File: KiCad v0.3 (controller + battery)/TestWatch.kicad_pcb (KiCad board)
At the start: 2 copper layers, 117 x 47.5 mm, 203 parts, among them J1 Conn_01x16

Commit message: Major Udpate 2
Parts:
- removed J1: Conn_01x16, Connector_PinHeader_1.00mm:PinHeader_1x16_P1.00mm_Vertical
- added Pogo2: Pogo2, WL-SMCC_0402:Untitled, F.Cu at (173.6, 99.5)
- added REF**: XTAL_MC-306_32.7680K-E0_PURE_SN, MC-306_32.7680K-E0_PURE_SN:MC-306_32.7680K-E0_PURE_SN, F.Cu at (197.0, 111.0)
- added REF**: BAT_BAT-HLD-003-SMT, BAT-HLD-003-SMT:BAT_BAT-HLD-003-SMT, F.Cu at (193.5, 92.5)
- added REF**: SW_EVQ-P7K01P_PAN, EVQ_P7K01P:EVQ_P7K01P, F.Cu at (205.5, 99.3)
- added REF**: LIR2050, WL-SMCC_0402:Untitled_1, F.Cu at (194.0, 92.5)
- moved IC** 11.9 mm to (187.5, 109.5)
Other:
- board size 117 x 47.5 mm -> 73 x 36.5 mm

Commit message: Uhm
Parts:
- removed D1, D10, D100, D101, D102, D103, D104, D105, D106, D107, D108, D109, D11, D110, D111, D112, D113, D114, D115, D116, D117, D118, D119, D12, D120, D121, D122, D123, D124, D125, D126, D127, D128, D129, D13, D130, D131, D132, D133, D134, D135, D136, D137, D138, D139, D14, D140, D141, D142, D143, D144, D145, D146, D147, D148, D149, D15, D150, D151, D152, D153, D154, D155, D156, D157, D158, D159, D16, D160, D161, D162, D163, D164, D165, D166, D167, D168, D169, D17, D170, D171, D172, D173, D174, D175, D176, D177, D178, D179, D18, D180, D181, D182, D183, D184, D185, D186, D187, D188, D189, D19, D190, D191, D192, D193, D194, D195, D196, D197, D198, D199, D2, D20, D200, D201, D21, D22, D23, D24, D25, D26, D27, D28, D29, D3, D30, D31, D32, D33, D34, D35, D36, D37, D38, D39, D4, D40, D41, D42, D43, D44, D45, D46, D47, D48, D49, D5, D50, D51, D52, D53, D54, D55, D56, D57, D58, D59, D6, D60, D61, D62, D63, D64, D65, D66, D67, D68, D69, D7, D70, D71, D72, D73, D74, D75, D76, D77, D78, D79, D8, D80, D81, D82, D83, D84, D85, D86, D87, D88, D89, D9, D90, D91, D92, D93, D94, D95, D96, D97, D98, D99: WL-SMCC_0402, WL-SMCC_0402:WL-SMCC_0402
- removed IC**: QFP80P900X900X160-32N, STM32G431KBT6:QFP80P900X900X160-32N
- removed Pogo2: Pogo2, WL-SMCC_0402:Untitled
- removed REF**: XTAL_MC-306_32.7680K-E0_PURE_SN, MC-306_32.7680K-E0_PURE_SN:MC-306_32.7680K-E0_PURE_SN
- removed REF**: BAT_BAT-HLD-003-SMT, BAT-HLD-003-SMT:BAT_BAT-HLD-003-SMT
- removed REF**: SW_EVQ-P7K01P_PAN, EVQ_P7K01P:EVQ_P7K01P
- removed REF**: LIR2050, WL-SMCC_0402:Untitled_1
- added BT1: BAT-HLD-003-SMT, BAT-HLD-003-SMT:BAT_BAT-HLD-003-SMT_CUT, F.Cu at (192.0, 93.5)
- added BUTT1: B3U-1100P, B3U_1100P:SW_B3U-1100P, F.Cu at (206.0, 99.5)
- added C1: GRM21BC81E106ME51K, GRM21BC81E106ME51K:CAPC2012X140N, F.Cu at (196.0, 115.5)
- added CHG1: MCP73832T-2ACI_OT, MCP73832T_2ACI_OT:SOT95P270X145-5N, F.Cu at (190.0, 105.4)
- added CUT1: MAX809SEUR_T, MAX809SEUR+T:MAX809SEUR+T, F.Cu at (180.1, 109.6)
- added J1: Conn_01x16, Connector_PinSocket_2.54mm:PinSocket_1x16_P2.54mm_Vertical, F.Cu at (180.5, 68.5)
- added Osc1: MC-306_32.7680K-E0_PURE_SN, MC-306_32.7680K-E0_PURE_SN:MC-306_32.7680K-E0_PURE_SN, F.Cu at (190.0, 113.0)
- added P13: ~, WL-SMCC_0402:PROGPAD, F.Cu at (206.0, 91.5)
- added P14: ~, WL-SMCC_0402:PROGPAD, F.Cu at (206.0, 94.5)
- added POGO1: ~, WL-SMCC_0402:Untitled, F.Cu at (173.1, 99.5)
- added Q1: IRLML6402, Package_TO_SOT_SMD:SOT-23, F.Cu at (184.5, 108.0)
- added R1: RN73H1JTTD5052F50, RN73H1JTTD5052F50:RN73H1JTTD5052F50, F.Cu at (185.5, 104.5)
- added R2: RN73H1JTTD5052F50, RN73H1JTTD5052F50:RN73H1JTTD5052F50, F.Cu at (206.5, 106.0)
- added R3: RN73H1JTTD5052F50, RN73H1JTTD5052F50:RN73H1JTTD5052F50, F.Cu at (182.0, 104.5)
- added REG1: TPS7A0225PDBVR, TPS7A0225PDBVR:TPS7A0225PDBVR, F.Cu at (184.4, 112.1)
- added STM1: STM32G431KBT6, STM32G431KBT6:QFP80P900X900X160-32N, F.Cu at (198.8, 108.7)
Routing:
- net A: track 79.8 -> 0.00 mm, vias 12 -> 0
- net E: track 78.5 -> 0.00 mm, vias 10 -> 0
- net B: track 77.9 -> 0.00 mm, vias 12 -> 0
- net F: track 77.5 -> 0.00 mm, vias 11 -> 0
- net G: track 76.5 -> 0.00 mm, vias 8 -> 0
- net H: track 75.0 -> 0.00 mm, vias 9 -> 0
- net C: track 74.8 -> 0.00 mm, vias 12 -> 0
- net I: track 72.8 -> 0.00 mm, vias 6 -> 0
- net J: track 72.8 -> 0.00 mm, vias 7 -> 0
- net D: track 72.5 -> 0.00 mm, vias 12 -> 0
- net L: track 71.5 -> 0.00 mm, vias 5 -> 0
- net K: track 66.4 -> 0.00 mm
- net P: track 64.9 -> 0.00 mm
- net O: track 62.5 -> 0.00 mm
- net N: track 60.1 -> 0.00 mm
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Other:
- board size 73 x 36.5 mm -> 45 x 52 mm

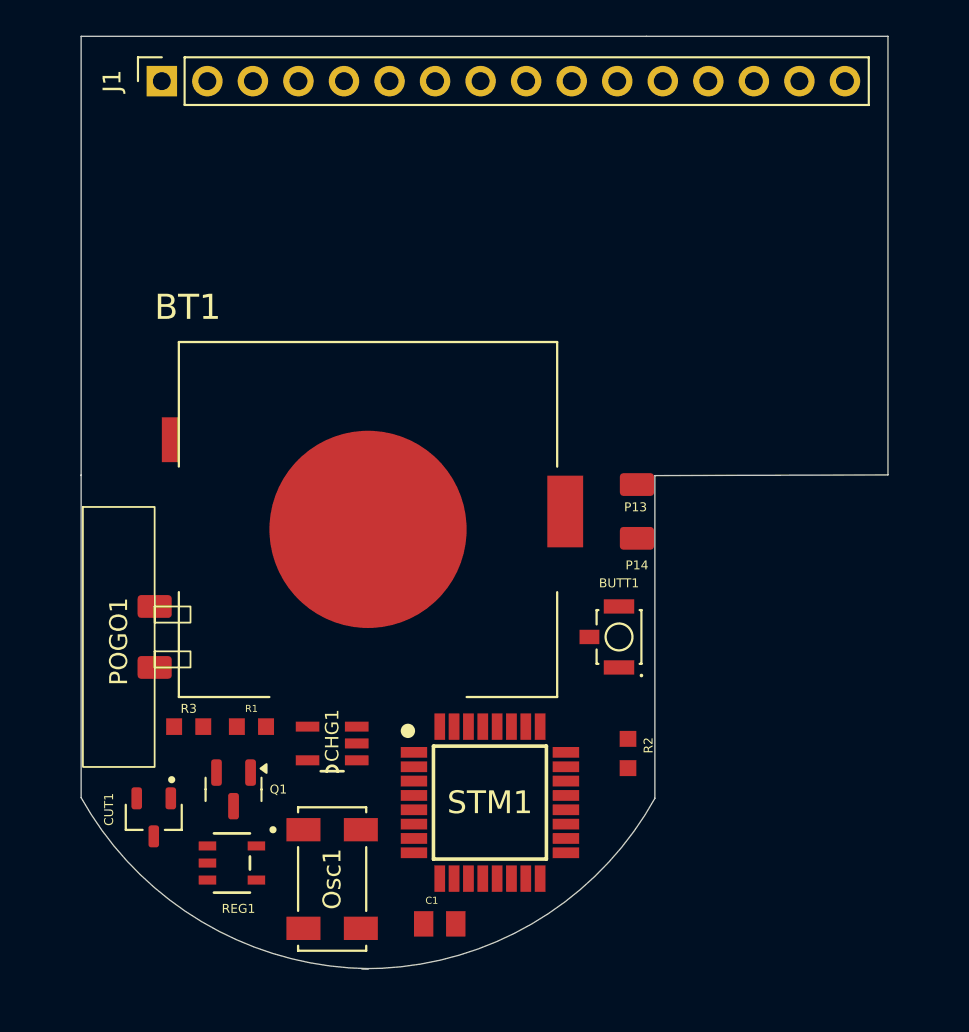
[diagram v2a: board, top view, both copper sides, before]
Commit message: v0.3 sent for fab, v0.4 still in progress
v0.3 and v0.4 have the same component footprints - that way, I only need to have 1 stencil (if v0.3 works!!!)
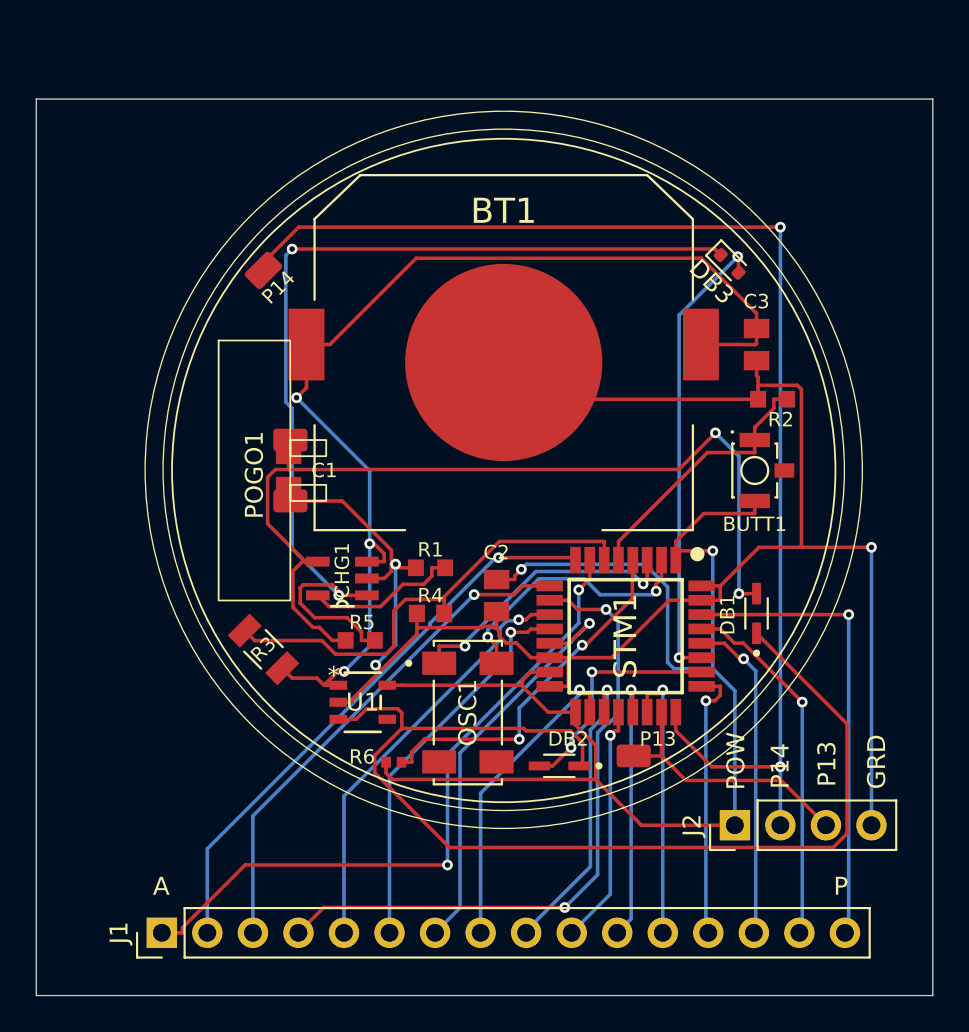
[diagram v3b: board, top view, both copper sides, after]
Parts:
- removed CUT1: MAX809SEUR_T, MAX809SEUR+T:MAX809SEUR+T
- removed Osc1: MC-306_32.7680K-E0_PURE_SN, MC-306_32.7680K-E0_PURE_SN:MC-306_32.7680K-E0_PURE_SN
- removed Q1: IRLML6402, Package_TO_SOT_SMD:SOT-23
- removed REG1: TPS7A0225PDBVR, TPS7A0225PDBVR:TPS7A0225PDBVR
- added C2: GRM21BC81E106ME51K, GRM21BC81E106ME51K:CAPC2012X140N, F.Cu at (199.2, 97.2)
- added C3: GRM21BC81E106ME51K, GRM21BC81E106ME51K:CAPC2012X140N, F.Cu at (213.7, 83.2)
- added DB1: BAS3010A03WE6327HTSA1, BAS3010A03WE6327HTSA1:SOD2513X110N, F.Cu at (213.7, 98.2)
- added DB2: BAS3010A03WE6327HTSA1, BAS3010A03WE6327HTSA1:SOD2513X110N, F.Cu at (202.7, 106.7)
- added DB3: 1N4148WT, Diode_SMD:D_SOD-523, F.Cu at (212.2, 78.7)
- added J2: Conn_01x04, Connector_PinHeader_2.54mm:PinHeader_1x04_P2.54mm_Vertical, F.Cu at (212.5, 110.0)
- added OSC1: MC-306_32.7680K-E0_PURE_SN, MC-306_32.7680K-E0_PURE_SN:MC-306_32.7680K-E0_PURE_SN, F.Cu at (197.6, 103.7)
- added R4: RMCF0603FT300K, RMCF0603FT300K:RMCF0603FT300K, F.Cu at (195.5, 98.2)
- added R5: RN73H1JTTD5052F50, RN73H1JTTD5052F50:RN73H1JTTD5052F50, F.Cu at (191.6, 99.7)
- added R6: RC1005F103CS, RC1005F103CS:RESC1005X40N, F.Cu at (193.4, 106.5)
- added U1: TPS7A0230PDBVR, TPS7A0230PDBVR:TPS7A0230PDBVR, F.Cu at (191.7, 103.1)
- J1: footprint Connector_PinSocket_2.54mm:PinSocket_1x16_P2.54mm_Vertical -> Connector_PinHeader_2.54mm:PinHeader_1x16_P2.54mm_Vertical
- R3: value RN73H1JTTD5052F50 -> RC1206FR-07120KL; footprint RN73H1JTTD5052F50:RN73H1JTTD5052F50 -> RC1206FR_07120KL:RC1206FR_07120KL
- moved J1 47.5 mm to (180.5, 116.0)
- moved C1 26.7 mm to (187.6, 90.2), turned to -90 degrees
- moved P14 24.8 mm to (185.8, 80.1), turned to 45 degrees
- moved R2 21.3 mm to (214.6, 86.2), turned to 180 degrees
- moved P13 15.1 mm to (205.8, 106.6)
- moved R1 13.3 mm to (195.5, 95.6)
- moved BUTT1 12.0 mm to (213.6, 90.2), turned to 90 degrees
- moved POGO1 12.0 mm to (180.7, 90.2)
- moved STM1 12.0 mm to (206.4, 99.5), turned to -90 degrees
- moved BT1 11.9 mm to (199.6, 84.3)
- moved CHG1 9.22 mm to (190.6, 96.2)
- moved R3 5.99 mm to (186.2, 100.2), turned to 135 degrees
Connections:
- net USB - renamed GNDREF
- C1 pad 1: Net-(CHG1-VDD) -> USB + 
- CHG1 pad 1: unconnected-(CHG1-STAT-Pad1) -> Net-(CHG1-STAT)
- CHG1 pad 3: BATT -> Net-(CHG1-VBAT)
- CHG1 pad 4: Net-(CHG1-VDD) -> USB + 
- P13 pad 1: Net-(STM1-PA14) -> Net-(J2-Pin_3)
- P14 pad 1: Net-(STM1-PA13) -> Net-(J2-Pin_2)
- R3 pad 1: USB +  -> Net-(CHG1-VBAT)
- R3 pad 2: Net-(Q1-G) -> Net-(STM1-PA1)
- STM1 pad 13: Net-(Q1-G) -> G
- STM1 pad 18: G -> H
- STM1 pad 19: H -> I
- STM1 pad 20: I -> J
- STM1 pad 21: J -> K
- STM1 pad 22: K -> L
- STM1 pad 23: Net-(STM1-PA13) -> Net-(J2-Pin_3)
- STM1 pad 24: Net-(STM1-PA14) -> Net-(J2-Pin_2)
- STM1 pad 25: L -> M
- STM1 pad 26: M -> Net-(STM1-PB3)
- STM1 pad 27: N -> Net-(DB3-A)
- STM1 pad 28: O -> N
- STM1 pad 29: P -> O
- STM1 pad 30: unconnected-(STM1-PB7-Pad30) -> P
- STM1 pad 4: unconnected-(STM1-PG10-NRST-Pad4) -> Net-(STM1-PG10-NRST)
- STM1 pad 6: STM_POW -> Net-(STM1-PA1)
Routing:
- net GNDREF: track 0.00 -> 103.6 mm, vias 0 -> 3
- net STM_POW: track 0.00 -> 80.7 mm, vias 0 -> 2
- net Net-(J2-Pin_2): track 0.00 -> 71.1 mm, vias 0 -> 2
- net Net-(CHG1-VBAT): track 0.00 -> 61.3 mm, vias 0 -> 3
- net Net-(U1-EN): track 0.00 -> 61.3 mm
- net Net-(CHG1-STAT): track 0.00 -> 55.1 mm, vias 0 -> 2
- net USB + : track 0.00 -> 51.1 mm, vias 0 -> 2
- net A: track 0.00 -> 38.0 mm, vias 0 -> 2
- net D: track 0.00 -> 37.0 mm, vias 0 -> 2
- net B: track 0.00 -> 32.1 mm, vias 0 -> 1
- net C: track 0.00 -> 28.4 mm, vias 0 -> 1
- net Net-(STM1-PA1): track 0.00 -> 26.2 mm
- net P: track 0.00 -> 26.0 mm, vias 0 -> 1
- net Net-(DB3-A): track 0.00 -> 25.9 mm, vias 0 -> 2
- net E: track 0.00 -> 23.7 mm, vias 0 -> 1
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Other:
- board size 45 x 52 mm -> 50 x 50 mm
- board text added: "A"
- board text added: "GRD"
- board text added: "P"
- board text added: "P13"
- board text added: "P14"
- board text added: "POW"
